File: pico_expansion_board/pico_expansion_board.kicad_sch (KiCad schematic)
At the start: 36 parts, among them J1 TMC2209 Motor 1, J2 TMC2209 Motor 2, J3 DC12V/24V, J4 A&D FX DB9, J5 A&D FX DB9_INV, J6 EXP1, J6 Motor 1, J7 EXP2, J7 Motor 2, U1 Pico, U2 TPS5430DDA, U3 MAX232

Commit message: Add external eeprom
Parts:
- added U4: AT24CS08-XHM, Package_SO:TSSOP-8_4.4x3mm_P0.65mm, symbol Memory_EEPROM:AT24CS08-XHM
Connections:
- net +5V: now also U4.8 (VCC)
- net GND: now also U4.3 (A2), U4.4 (GND), U4.7 (WP)
- net MOTOR_UART: now also R3.1; no longer R3.2
- net SCALE_UART_RX: now also U1.1 (GPIO0); no longer U1.6 (GPIO4)
- net EEPROM_SDA: now reaches U1.14 (GPIO10)
- net EEPROM_SDA: now also U4.5 (SDA)
- net EEPROM_SCL: now reaches U1.15 (GPIO11)
- net EEPROM_SCL: now also U4.6 (SCL)
- removed net UART0_TX: R3.1, U1.1 (GPIO0)
- new net UART1_TX: R3.2, U1.6 (GPIO4)
- no-connect marks 4 -> 32
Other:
- note added: "EEPROM"
- note added: "Rasberry Pi Pico/W Expansion Board"
- note added: "Raspberry Pico/W Expansion Board For OpenTricker RP2040 Controller"
- moved on the sheet: J6, J7, R3

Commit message: Update PCB and schematic design
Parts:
- removed C1: 4.7uF, symbol Device:C
- removed C4: 220uF, symbol Device:C_Polarized_Small_US
- removed D1, D2: B340, Diode_SMD:D_SMC, symbol Diode:B340
- removed L1: 22uH, symbol Device:L
- removed R2: 3.24K, symbol Device:R
- removed U2: TPS5430DDA, Package_SO:TI_SO-PowerPAD-8_ThermalVias, symbol Regulator_Switching:TPS5430DDA
- added C10, C11: 4.7uF, Capacitor_SMD:C_0805_2012Metric, symbol Device:C
- added C12, C13, C15: 0.01uF, Capacitor_SMD:C_0805_2012Metric, symbol Device:C
- added C14: 220uF, Capacitor_SMD:CP_Elec_10x10.5, symbol Device:C_Polarized_Small_US
- added D3: SS54, DO-214AC, symbol SS54:SS54
- added H1, H2, H3, H4: MountingHole, MountingHole:MountingHole_3.2mm_M3_Pad_Via, symbol Mechanical:MountingHole
- added J10: CAN_L, TerminalBlock:TerminalBlock_bornier-2_P5.08mm, symbol Connector:Screw_Terminal_01x02
- added JP9: TX_OP2, Connector_PinHeader_2.54mm:PinHeader_1x02_P2.54mm_Vertical, symbol Jumper:Jumper_2_Open
- added L2: 15uH, Inductor_SMD:L_Vishay_IHLP-4040, symbol Device:L
- added R4: 10K, Resistor_SMD:R_0805_2012Metric, symbol Device:R
- added R5: 3.16K, Resistor_SMD:R_0805_2012Metric, symbol Device:R
- added SW1: SW_Push, Button_Switch_SMD:SW_Push_1P1T_NO_6x6mm_H9.5mm, symbol Switch:SW_Push
- added TP2, TP3, TP4, TP5, TP7, TP8: TestPoint, TestPoint:TestPoint_Pad_2.0x2.0mm, symbol Connector:TestPoint
- added U2: MCP2542FDxMF, Package_DFN_QFN:DFN-8-1EP_3x3mm_P0.65mm_EP1.55x2.4mm, symbol Interface_CAN_LIN:MCP2542FDxMF
- added U5: TPS5450DDAR, CONV_TPS5450DDAR, symbol TPS5450DDAR:TPS5450DDAR
- C1: renamed from C5; footprint (none) -> Capacitor_SMD:C_0805_2012Metric
- C2: value 4.7uF -> 0.1uF; footprint (none) -> Capacitor_SMD:C_0805_2012Metric
- C3: value 0.01uF -> 0.1uF; footprint (none) -> Capacitor_SMD:C_0805_2012Metric
- C4: renamed from C9; footprint (none) -> Capacitor_SMD:C_0805_2012Metric
- C6: footprint (none) -> Capacitor_SMD:C_0805_2012Metric
- C7: renamed from C8; footprint (none) -> Capacitor_SMD:C_0805_2012Metric
- C8: renamed from C7; footprint (none) -> Capacitor_SMD:C_0805_2012Metric
- J1: renamed from J3; footprint (none) -> TerminalBlock:TerminalBlock_bornier-2_P5.08mm
- J4: renamed from J6; footprint (none) -> Connector_JST:JST_XH_B4B-XH-AM_1x04_P2.50mm_Vertical
- J5: renamed from J7; footprint (none) -> Connector_JST:JST_XH_B4B-XH-AM_1x04_P2.50mm_Vertical
- J6: renamed from J5; footprint (none) -> Connector_Dsub:DSUB-9_Male_Horizontal_P2.77x2.84mm_EdgePinOffset7.70mm_Housed_MountingHolesOffset9.12mm
- J7: renamed from J4; footprint (none) -> Connector_Dsub:DSUB-9_Male_Horizontal_P2.77x2.84mm_EdgePinOffset7.70mm_Housed_MountingHolesOffset9.12mm
- J8: renamed from J6; footprint (none) -> Connector_IDC:IDC-Header_2x05_P2.54mm_Vertical
- J9: renamed from J7; footprint (none) -> Connector_IDC:IDC-Header_2x05_P2.54mm_Vertical
- JP1: renamed from JP5; footprint (none) -> Connector_PinHeader_2.54mm:PinHeader_1x02_P2.54mm_Vertical
- JP2: renamed from JP6; footprint (none) -> Connector_PinHeader_2.54mm:PinHeader_1x02_P2.54mm_Vertical
- JP3: renamed from JP7; footprint (none) -> Connector_PinHeader_2.54mm:PinHeader_1x02_P2.54mm_Vertical
- JP4: renamed from JP8; footprint (none) -> Connector_PinHeader_2.54mm:PinHeader_1x02_P2.54mm_Vertical
- JP5: renamed from JP3; footprint (none) -> Connector_PinHeader_2.54mm:PinHeader_1x02_P2.54mm_Vertical
- JP6: renamed from JP4; footprint (none) -> Connector_PinHeader_2.54mm:PinHeader_1x02_P2.54mm_Vertical
- JP7: renamed from JP1; footprint (none) -> Connector_PinHeader_2.54mm:PinHeader_1x02_P2.54mm_Vertical
- JP8: renamed from JP2; footprint (none) -> Connector_PinHeader_2.54mm:PinHeader_1x02_P2.54mm_Vertical
- R1, R3: footprint (none) -> Resistor_SMD:R_0805_2012Metric
- TP1: value BOOT -> TestPoint; footprint (none) -> TestPoint:TestPoint_Pad_2.0x2.0mm
- U1: renamed from U3; footprint (none) -> Package_SO:SOIC-16_3.9x9.9mm_P1.27mm
- renumbered J1 to J2, J2 to J3, U1 to U3
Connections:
- net VDD is gone; now on net VCC: J2.9 (VM), J3.9 (VM)
- net +3.3V: now also C2.2, U2.5 (VIO)
- net +5V: now also C3.1, C14.1, C15.1, L2.2, R4.1, U2.3 (VDD); no longer R1.1
- net GND: now also C2.1, C3.2, J6.0 (PAD), C10.2, C11.2, C12.2, C14.2, C15.2, D3.A, R5.2, SW1.2, U2.2 (VSS), U2.8 (STBY), U2.9 (VSS), U5.6 (GND), U5.9 (POWERPAD); no longer C2.2
- net MOTOR_UART: now also U3.7 (GPIO5), TP4.1; no longer U3.2 (GPIO1)
- net NEOPIXEL: now also U3.31 (GPIO26_ADC0); no longer U3.17 (GPIO13)
- net SCALE_RXD: now also TP2.1
- net SCALE_TXD: now also TP1.1
- net SCALE_UART_RX: now also TP8.1
- net SCALE_UART_TX: now also U3.2 (GPIO1), TP7.1; no longer U3.7 (GPIO5)
- net VCC: now also C10.1, C11.1, C12.1, TP3.1, U5.7 (VIN)
- net at R1.2: now also J10.2 (Pin_2), U2.6 (CANL)
- net PICO_RESET_BTN: now reaches U3.30 (RUN)
- net PICO_RESET_BTN: now also SW1.1
- net CAN_TX: now reaches U3.32 (GPIO27_ADC1)
- net CAN_TX: now also U2.1 (TXD)
- net CAN_RX: now reaches U3.34 (GPIO28_ADC2)
- net CAN_RX: now also U2.4 (RXD)
- new net: JP9.1 (A), R1.1
- new net: R4.2, R5.1, U5.4 (VSENSE)
- new net: TP5.1, U3.17 (GPIO13)
- new net: J10.1 (Pin_1), JP9.2 (B), U2.7 (CANH)
- new net: C13.2, D3.C, L2.1, U5.8 (PH)
- new net: C13.1, U5.1 (BOOT)
- no-connect marks 32 -> 31
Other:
- note added: "CAN Transceiver"
- note added: "Mounting Hardware"
- note added: "Power Control"
- moved on the sheet: R3

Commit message: Update design
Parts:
- removed C10, C11: 4.7uF, Capacitor_SMD:C_0805_2012Metric, symbol Device:C
- removed C12, C13, C15: 0.01uF, Capacitor_SMD:C_0805_2012Metric, symbol Device:C
- removed C14: 220uF, Capacitor_SMD:CP_Elec_10x10.5, symbol Device:C_Polarized_Small_US
- removed D3: SS54, DO-214AC, symbol SS54:SS54
- removed JP5: TX_OP2, Connector_PinHeader_2.54mm:PinHeader_1x02_P2.54mm_Vertical, symbol Jumper:Jumper_2_Open
- removed JP6: RX_OP2, Connector_PinHeader_2.54mm:PinHeader_1x02_P2.54mm_Vertical, symbol Jumper:Jumper_2_Open
- removed JP7: TX_OP1, Connector_PinHeader_2.54mm:PinHeader_1x02_P2.54mm_Vertical, symbol Jumper:Jumper_2_Open
- removed JP8: RX_OP1, Connector_PinHeader_2.54mm:PinHeader_1x02_P2.54mm_Vertical, symbol Jumper:Jumper_2_Open
- removed L2: 15uH, Inductor_SMD:L_Vishay_IHLP-4040, symbol Device:L
- removed R4: 10K, Resistor_SMD:R_0805_2012Metric, symbol Device:R
- removed R5: 3.16K, Resistor_SMD:R_0805_2012Metric, symbol Device:R
- removed TP3: TestPoint, TestPoint:TestPoint_Pad_2.0x2.0mm, symbol Connector:TestPoint
- removed U5: TPS5450DDAR, CONV_TPS5450DDAR, symbol TPS5450DDAR:TPS5450DDAR
- added C16, C17, C19: 10nF, Capacitor_SMD:C_0805_2012Metric, symbol Device:C
- added C18: 330uF, Capacitor_SMD:CP_Elec_10x10.5, symbol Device:C_Polarized_Small_US
- added C5, C9: 4.7uF, Capacitor_SMD:C_0805_2012Metric, symbol Device:C
- added D1: SS54, DO-214AC, symbol SS54:SS54
- added IC1: TPS5450DDA, SOIC127P600X170-9N, symbol TPS5450DDA:TPS5450DDA
- added L1: 15uH, Inductor_SMD:L_10.4x10.4_H4.8, symbol Device:L
- added R2: 10K, Resistor_SMD:R_0805_2012Metric, symbol Device:R
- added R6: 3.16K, Resistor_SMD:R_0805_2012Metric, symbol Device:R
- added TP6: TestPoint, TestPoint:TestPoint_Pad_2.0x2.0mm, symbol Connector:TestPoint
- C2, C3: value 0.1uF -> 100nF
- C4: value 0.1uF -> 1uF
- H1, H2, H3, H4: footprint MountingHole:MountingHole_3.2mm_M3_Pad_Via -> MountingHole:MountingHole_3.2mm_M3_Pad
- J6: value A&D FX DB9_INV -> Straight Through
- J7: value A&D FX DB9 -> NULL Modem
- JP1, JP2: footprint Connector_PinHeader_2.54mm:PinHeader_1x02_P2.54mm_Vertical -> Connector_PinHeader_2.00mm:PinHeader_1x02_P2.00mm_Vertical
- JP3, JP4: footprint Connector_PinHeader_2.54mm:PinHeader_1x02_P2.54mm_Vertical -> Connector_PinSocket_2.00mm:PinSocket_1x02_P2.00mm_Vertical
- JP9: value TX_OP2 -> 120JP; footprint Connector_PinHeader_2.54mm:PinHeader_1x02_P2.54mm_Vertical -> Connector_PinHeader_2.00mm:PinHeader_1x02_P2.00mm_Vertical
- R1: value 10K -> 120Ω
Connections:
- net +5V: now also C18.1, C19.1, L1.2, R2.1
- net GND: now also C16.2, C18.2, C19.2, C5.2, C9.2, D1.A, IC1.6 (GND), IC1.9 (EP), R6.2
- net SCALE_RXD: now also J6.2, J7.3
- net SCALE_TXD: now also J6.3, J7.2
- net VCC: now also C16.1, C5.1, C9.1, IC1.7 (VIN), TP6.1
- new net: C17.1, IC1.1 (BOOT)
- new net: C17.2, D1.C, IC1.8 (PH), L1.1
- new net: IC1.4 (VSENSE), R2.2, R6.1
- no-connect marks 31 -> 33

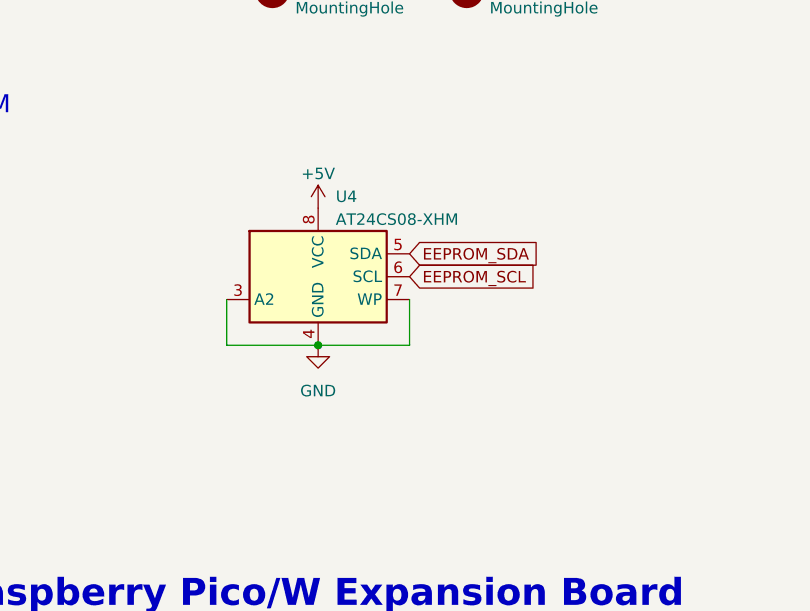
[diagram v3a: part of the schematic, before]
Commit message: Add 3d models for pico and stepper drivers
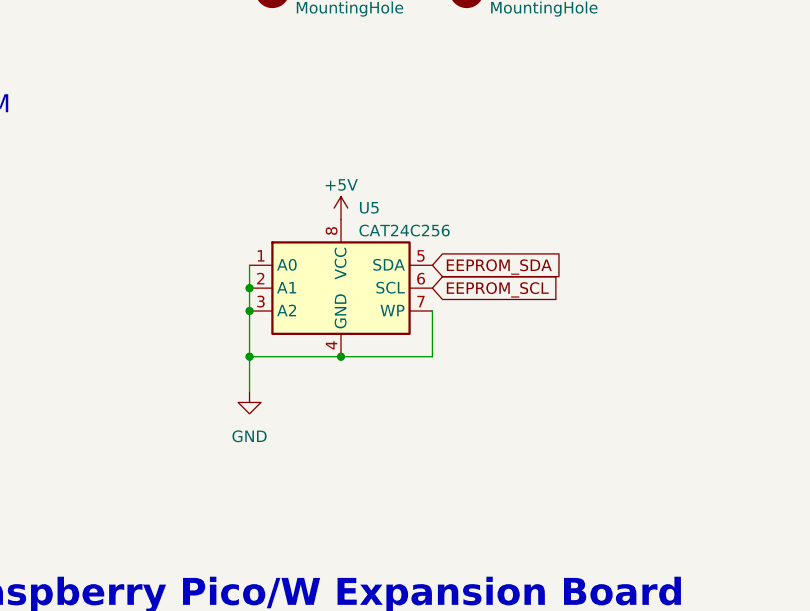
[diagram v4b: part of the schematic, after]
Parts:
- removed U4: AT24CS08-XHM, Package_SO:TSSOP-8_4.4x3mm_P0.65mm, symbol Memory_EEPROM:AT24CS08-XHM
- added U5: CAT24C256, Package_SO:SO-8_3.9x4.9mm_P1.27mm, symbol Memory_EEPROM:CAT24C256
- L1: footprint Inductor_SMD:L_10.4x10.4_H4.8 -> Extra Footprints:Power Inductor 10x11
- U2: footprint Package_DFN_QFN:DFN-8-1EP_3x3mm_P0.65mm_EP1.55x2.4mm -> Package_SO:SO-8_3.9x4.9mm_P1.27mm
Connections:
- net +5V: now also U5.8 (VCC)
- net EEPROM_SCL: now also U5.6 (SCL)
- net EEPROM_SDA: now also U5.5 (SDA)
- net GND: now also U5.1 (A0), U5.2 (A1), U5.3 (A2), U5.4 (GND), U5.7 (WP); no longer U2.9 (VSS)

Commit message: Update production file, update STEP models
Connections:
- net SCALE_UART_RX: now also U3.2 (GPIO1); no longer U3.1 (GPIO0)
- net SCALE_UART_TX: now also U3.1 (GPIO0); no longer U3.2 (GPIO1)
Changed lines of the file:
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@@
     )
   )
-  (global_label "UART0_RX" (shape input) (at 232.41 138.43 0) (fields_autoplaced)
+  (global_label "UART0_TX" (shape input) (at 232.41 138.43 0) (fields_autoplaced)
     (effects (font (size 1.27 1.27)) (justify left))
-    (property "Intersheetrefs" "${INTERSHEET_REFS}" (at 244.6291 138.43 0)
+    (property "Intersheetrefs" "${INTERSHEET_REFS}" (at 244.3267 138.43 0)
       (effects (font (size 1.27 1.27)) (justify left) hide)
     )
@@
     )
   )
-  (global_label "UART0_TX" (shape input) (at 232.41 142.24 0) (fields_autoplaced)
+  (global_label "UART0_RX" (shape input) (at 232.41 142.24 0) (fields_autoplaced)
     (effects (font (size 1.27 1.27)) (justify left))
-    (property "Intersheetrefs" "${INTERSHEET_REFS}" (at 244.3267 142.24 0)
+    (property "Intersheetrefs" "${INTERSHEET_REFS}" (at 244.6291 142.24 0)
       (effects (font (size 1.27 1.27)) (justify left) hide)
     )

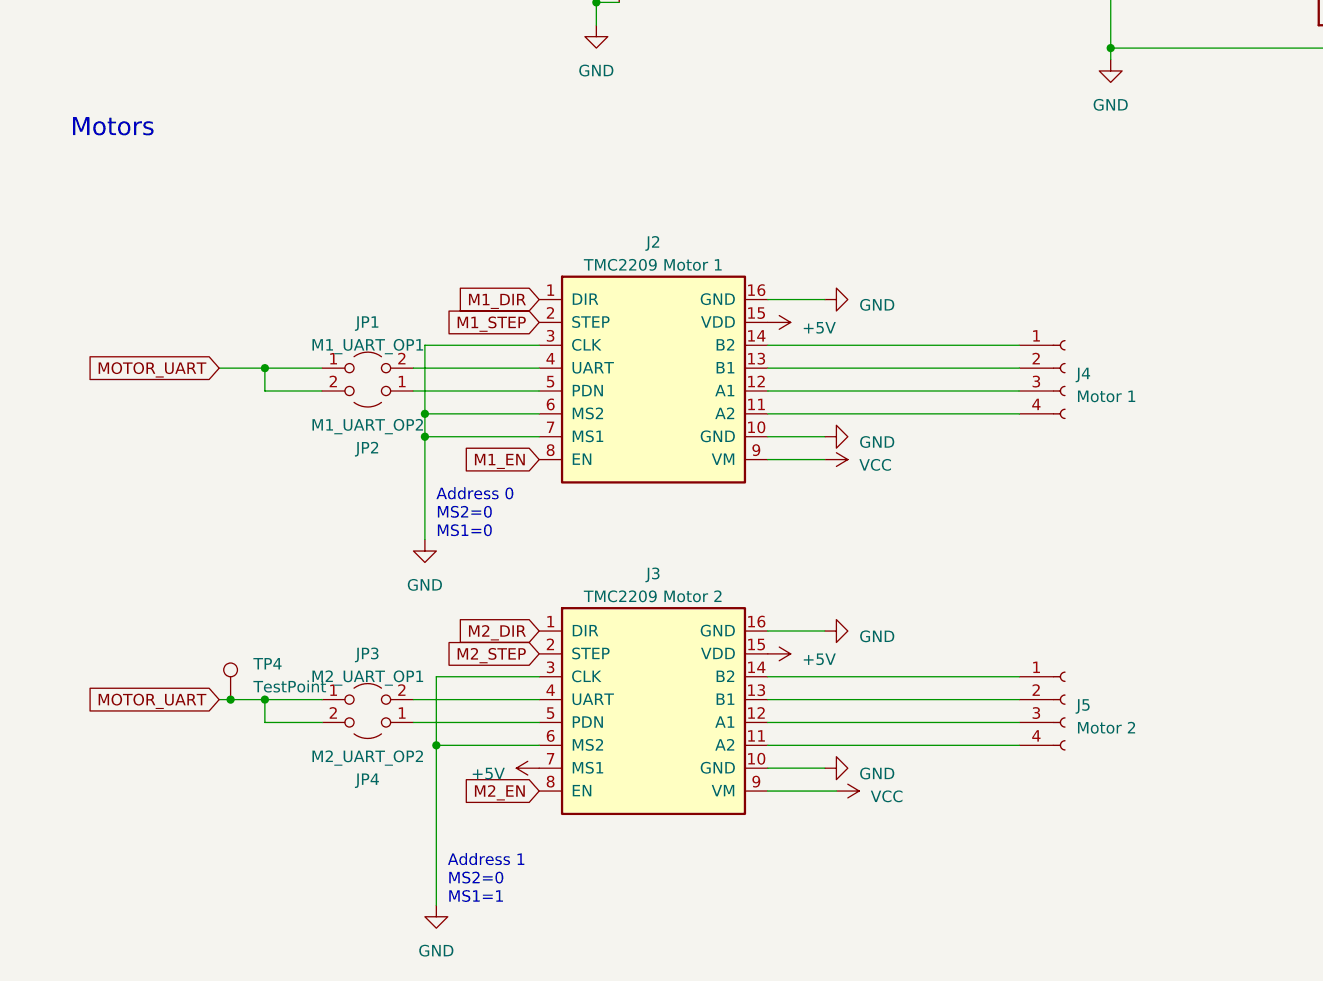
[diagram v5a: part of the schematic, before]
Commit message: Update to v0.2, include additional caps for StepStick driver VM input
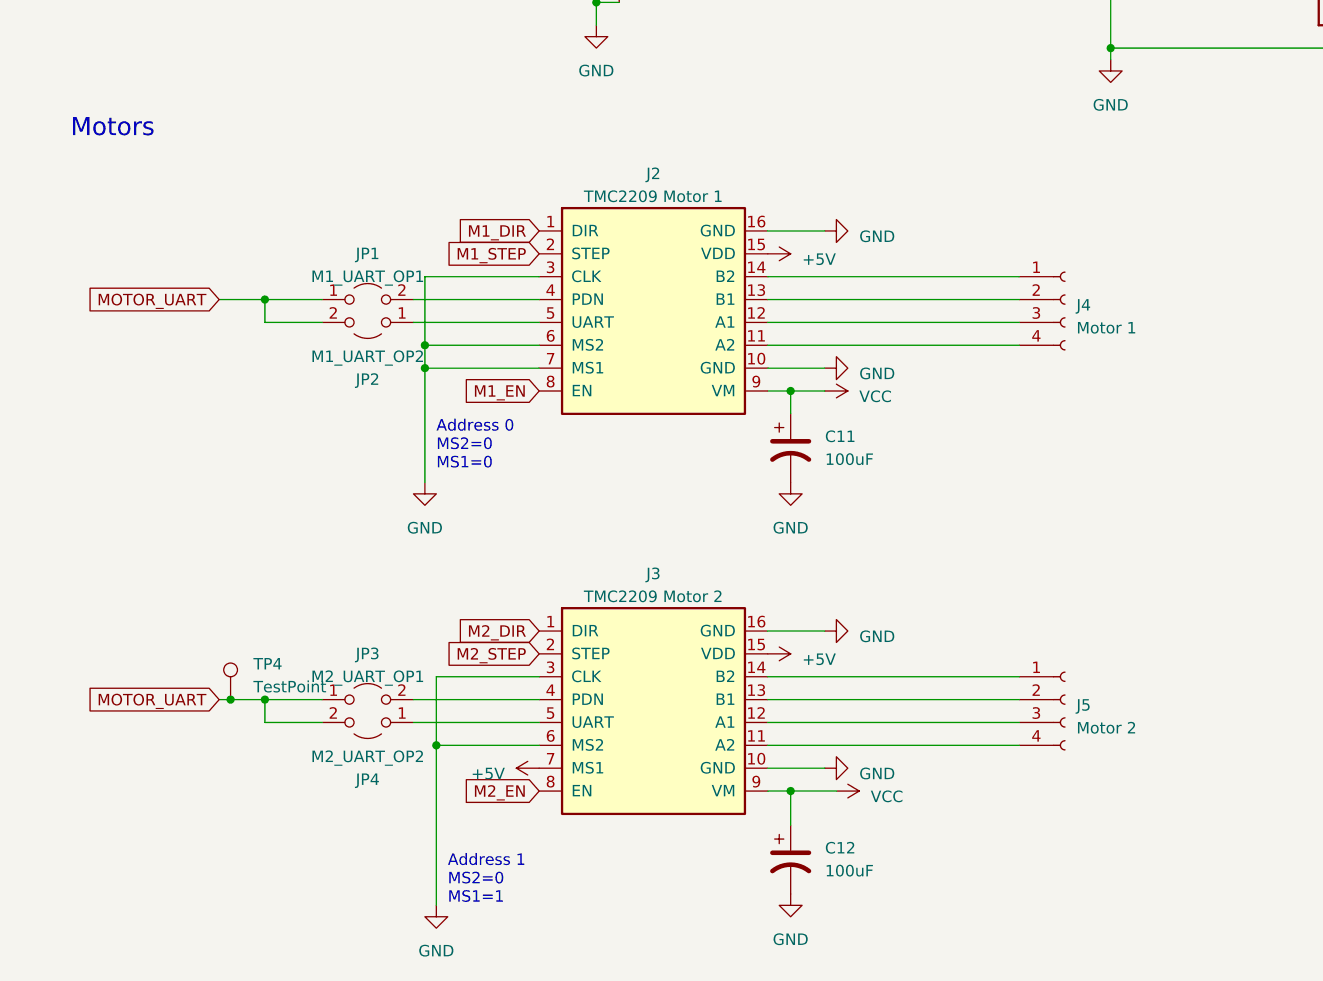
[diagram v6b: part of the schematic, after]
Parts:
- added C11, C12: 100uF, Capacitor_SMD:CP_Elec_6.3x7.7, symbol Device:C_Polarized_US
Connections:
- net GND: now also C11.2, C12.2
- net VCC: now also C11.1, C12.1
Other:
- moved on the sheet: J2, J4, JP1, JP2
